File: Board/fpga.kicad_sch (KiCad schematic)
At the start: 16 parts, among them U1 XC6SLX9-TQG144

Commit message: update
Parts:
- added R4: 330, Resistor_SMD:R_0603_1608Metric_Pad0.98x0.95mm_HandSolder, symbol Device:R
- R1: value 330 -> 4k7
- UX16: footprint cbm_ultipet_v1:PSOP-8-FIXED -> Package_SO:Diodes_PSOP-8
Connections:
- net GND: no longer C154.1, C155.1, C64.1, R1.1, R2.1, U1.129 (VCCAUX), U1.20 (VCCAUX), U1.36 (VCCAUX), U1.53 (VCCAUX), U1.90 (VCCAUX), UX16.2 (EN), UX17.2 (VO), UX18.7 (/HOLD), UX18.8 (VCC)
- net at U1.71 (DONE_2): now also R4.2
- new net V33: C154.1, C155.1, C64.1, R1.1, R2.1, R4.1, U1.129 (VCCAUX), U1.20 (VCCAUX), U1.36 (VCCAUX), U1.53 (VCCAUX), U1.90 (VCCAUX), UX16.2 (EN), UX17.2 (VO), UX18.7 (/HOLD), UX18.8 (VCC)
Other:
- moved on the sheet: JP1, R1

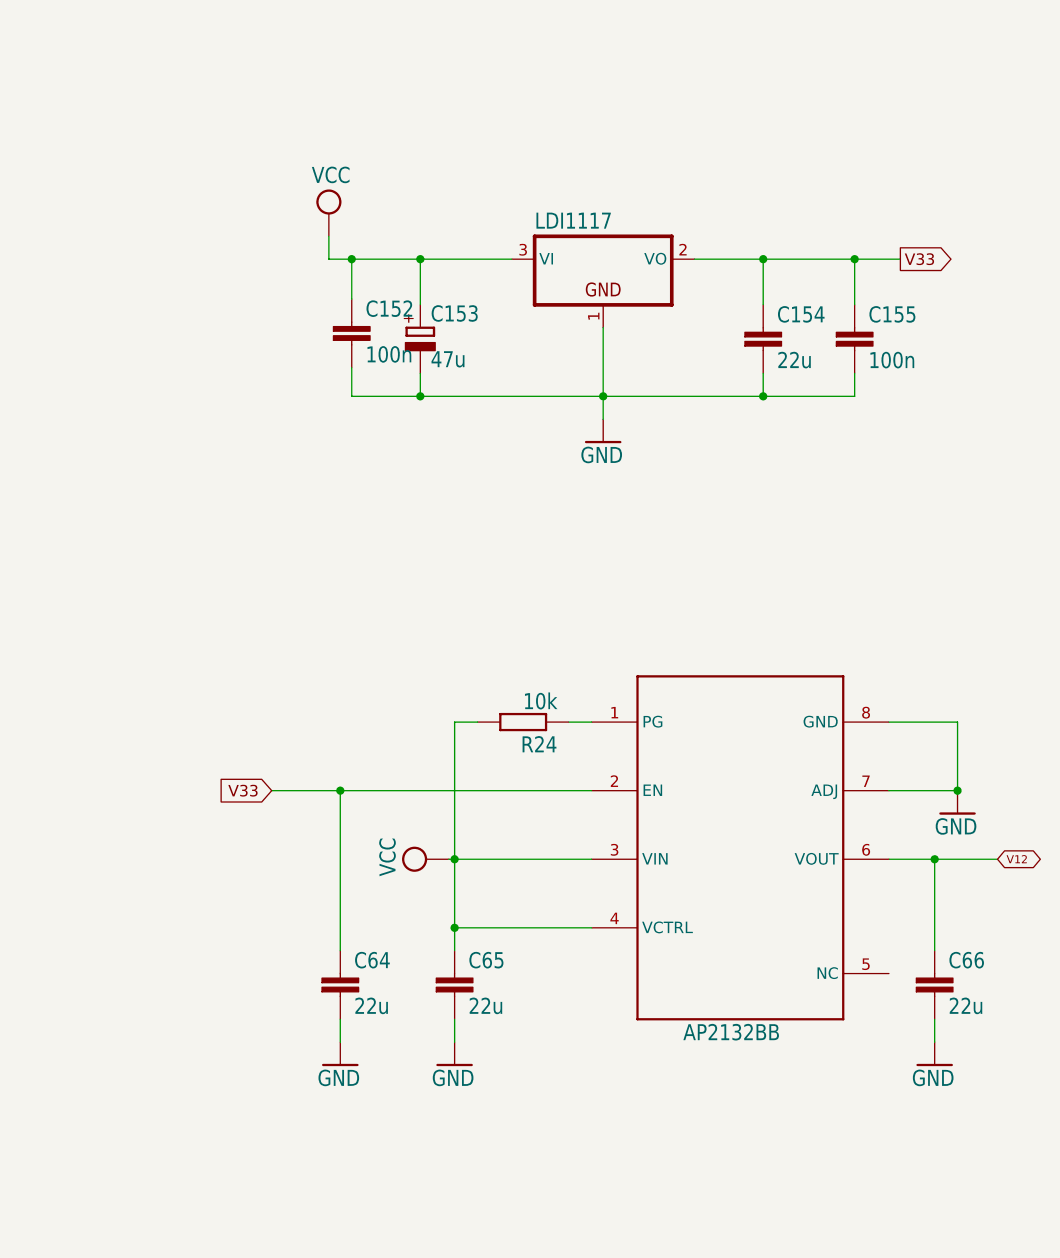
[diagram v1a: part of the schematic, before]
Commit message: adding keyboard, serial IEC
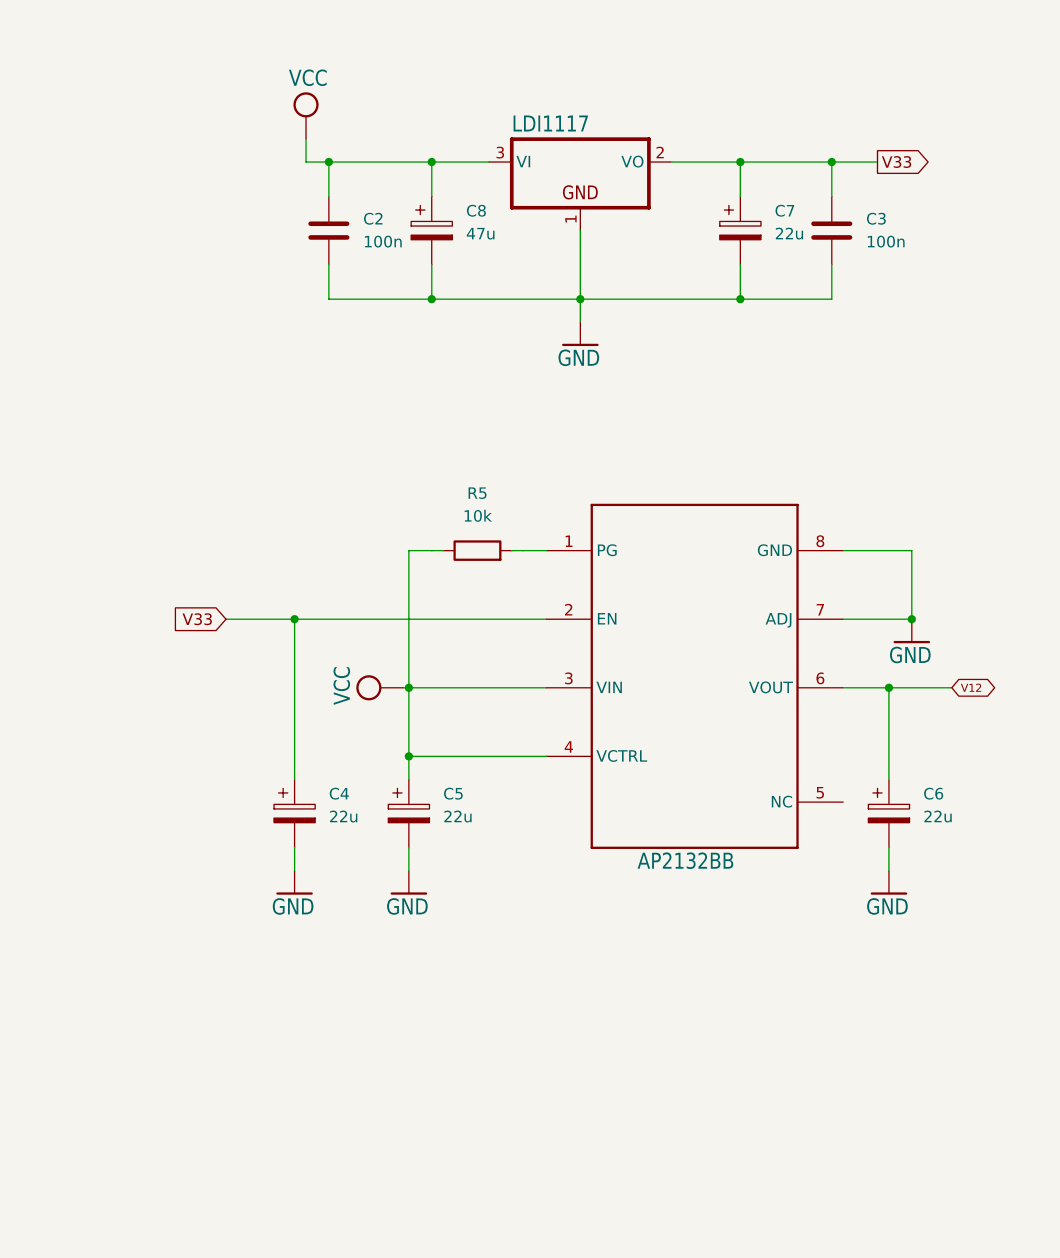
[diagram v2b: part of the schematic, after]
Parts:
- removed C152, C155: 100n, cbm_ultipet_v1:C0603, symbol cbm_ultipet_v1-eagle-import:C-EUC0603
- removed C153: 47u, cbm_ultipet_v1:E2,5-6, symbol cbm_ultipet_v1-eagle-import:CPOL-EUE2.5-6
- removed C154, C64, C65, C66: 22u, cbm_ultipet_v1:C0805, symbol cbm_ultipet_v1-eagle-import:C-EUC0805
- removed R24: 10k, cbm_ultipet_v1:0207_2V, symbol cbm_ultipet_v1-eagle-import:R-EU_0207/2V
- added C2, C3: 100n, Capacitor_SMD:C_0805_2012Metric, symbol Device:C
- added C4, C5, C6, C7: 22u, Capacitor_SMD:C_0805_2012Metric_Pad1.18x1.45mm_HandSolder, symbol Device:C_Polarized
- added C8: 47u, Capacitor_SMD:C_0805_2012Metric_Pad1.18x1.45mm_HandSolder, symbol Device:C_Polarized
- added R5: 10k, Resistor_SMD:R_0603_1608Metric_Pad0.98x0.95mm_HandSolder, symbol Device:R
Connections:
- net GND: now also C2.2, C3.2, C4.2, C5.2, C6.1, C6.2, C7.2, C8.2
- net V33: now also C3.1, C4.1, C7.1
- net VCC: now also C2.1, C5.1, C8.1, R5.1
- net at UX16.1 (PG): now also R5.2

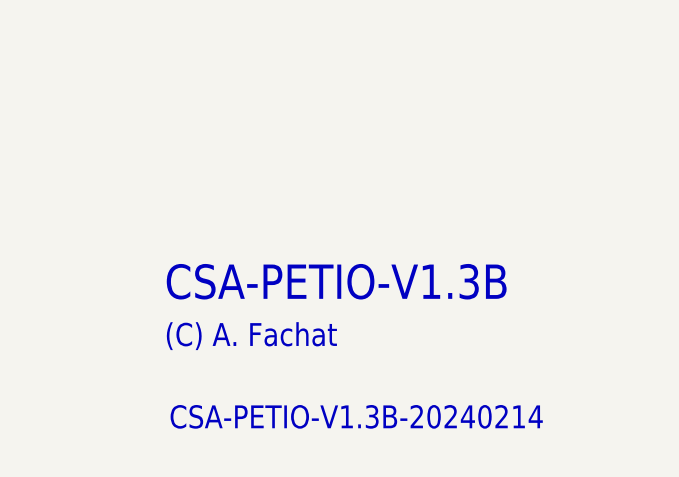
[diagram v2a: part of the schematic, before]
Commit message: add serial, SPI-10-5V
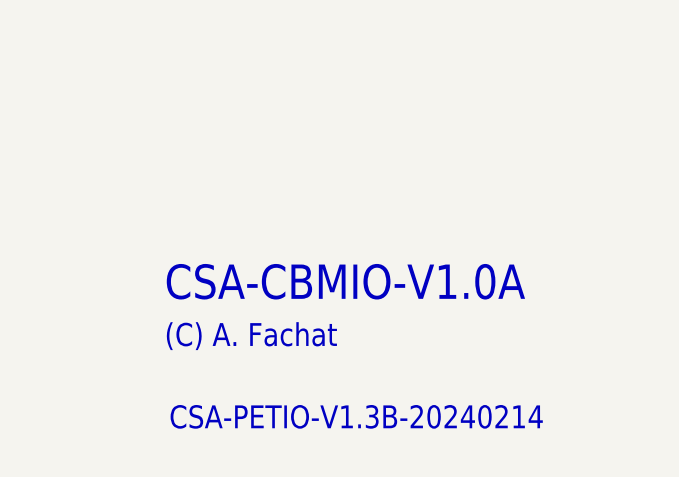
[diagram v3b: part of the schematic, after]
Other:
- note added: "CSA-CBMIO-V1.0A"
- note removed: "CSA-PETIO-V1.3B"
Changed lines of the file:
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@@
 	(generator_version "9.0")
 	(paper "A4")
-	(text "CSA-PETIO-V1.3B"
+	(text "CSA-CBMIO-V1.0A"
 		(exclude_from_sim no)
 		(at 206.756 172.72 0)

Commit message: schematics 1st full rev
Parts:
- added C10, C15, C16, C17, C18, C19, C20, C21, C23, C24, C25, C26, C9: 100n, Capacitor_SMD:C_0805_2012Metric, symbol Device:C
- added U21, U22: 74LVC1G125, Package_TO_SOT_SMD:SOT-353_SC-70-5, symbol 74xGxx:74LVC1G125
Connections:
- net GND: now also C10.2, C15.2, C16.2, C17.2, C18.2, C19.2, C20.2, C21.2, C23.2, C24.2, C25.2, C26.2, C9.2, U21.2, U21.3 (GND), U22.2, U22.3 (GND)
- net V33: now also C10.1, C15.1, C16.1, C17.1, C18.1, C19.1, C20.1, C21.1, C9.1, U21.5 (VCC), U22.5 (VCC)
- net VCC: now also C23.1, C24.1, C25.1, C26.1
- net at R4.2, U1.71 (DONE_2): now also U21.1, U22.1
- new net HSWAP: U22.4
- new net M1: U21.4
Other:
- note added: "CSA-CBMIO-V1.0A-20250815"
- note removed: "CSA-PETIO-V1.3B-20240214"

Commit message: full connect, starting on prod
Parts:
- added C1, C22, C27, C28, C29, C30, C31, C32, C33, C34, C35, C36, C37, C38, C39, C40: 100n, Capacitor_SMD:C_0805_2012Metric, symbol Device:C
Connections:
- net GND: now also C1.2, C22.2, C27.2, C28.2, C29.2, C30.2, C31.2, C32.2, C33.2, C34.2, C35.2, C36.2, C37.2, C38.2, C39.2, C40.2; no longer C6.1, U1.128 (VCCINT), U1.19 (VCCINT), U1.28 (VCCINT), U1.52 (VCCINT), U1.89 (VCCINT), UX16.6 (VOUT)
- net V33: now also C29.1, C30.1, C31.1, C32.1, C33.1, C34.1, C35.1, C36.1, C37.1, C38.1, C39.1, C40.1
- new net V12: C1.1, C22.1, C27.1, C28.1, C6.1, U1.128 (VCCINT), U1.19 (VCCINT), U1.28 (VCCINT), U1.52 (VCCINT), U1.89 (VCCINT), UX16.6 (VOUT)

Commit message: 1st working as 1.0B
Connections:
- net GND: now also UX7.10 (P$1), UX7.2 (GND)
- net V33: now also UX7.4 (VCC)
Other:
- note added: "1.0B: add GND and ref voltage to FPGA header"
- note added: "CSA-CBMIO-V1.0B"
- note added: "CSA-CBMIO-V1.0B-20260321"
- note removed: "CSA-CBMIO-V1.0A"
- note removed: "CSA-CBMIO-V1.0A-20250815"
